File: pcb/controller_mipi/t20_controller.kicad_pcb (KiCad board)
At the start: 2 copper layers, 48 parts, among them J1 M55-7002042R, J2 M55-7002042R, J3 1-84952-5, J4 1-84952-5, J5 0473093351, U10 MIC33153YHJ-TR, U13 NCP161BMX330TBG, U2 MIC33153YHJ-TR, U3 MIC5353-2.8YMT, U4 TPS22964CYZPR, U5 MIC5353-2.5YMT, U6 MIC5353-1.8YMT, U7 TPS22964CYZPR, U8 TPS22964CYZPR, U9 TPS22964CYZPR

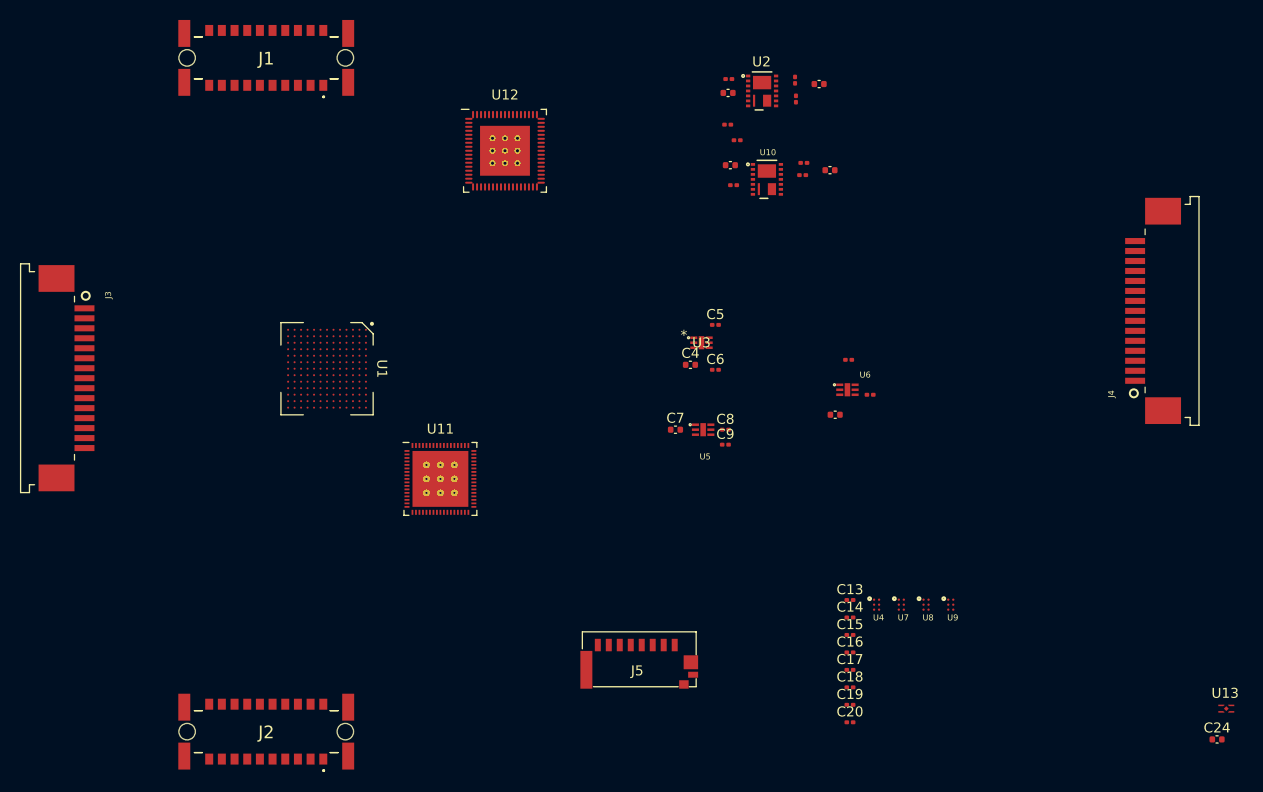
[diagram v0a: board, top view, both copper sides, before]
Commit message: 4 mipi connectors exposed
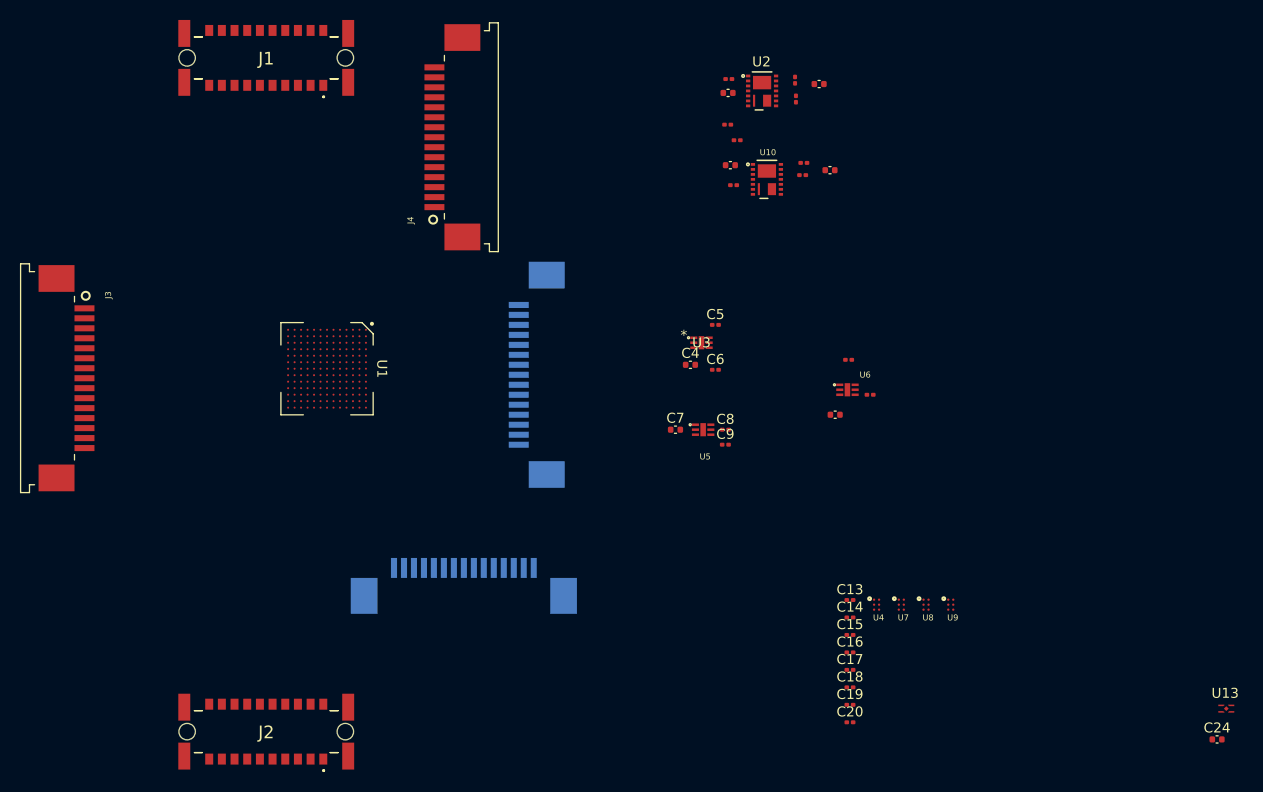
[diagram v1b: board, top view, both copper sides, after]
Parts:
- removed U11: ~, smd:QFN-68_EP_7x7_Pitch0.35mm
- removed U12: ~, smd:QFN-68_EP_8x8_Pitch0.4mm
- added J6: 1-84952-5, smd:TE_1-84952-5, B.Cu at (129.8, 118.3)
- J5: value 0473093351 -> 1-84952-5; footprint smd:0473093351 -> smd:TE_1-84952-5; moved to B.Cu
- moved J4 72.3 mm to (126.8, 75.2)
- moved J5 28.3 mm to (135.3, 99.0), turned to -90 degrees
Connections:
- J3 pad 11: unconnected-(J3-Pad11) -> /MIPI/MIPI0_TXD3_N
- J3 pad 12: unconnected-(J3-Pad12) -> /MIPI/MIPI0_TXD3_P
- J3 pad 13: unconnected-(J3-Pad13) -> GND
- J3 pad 14: unconnected-(J3-Pad14) -> /MIPI/MIPI0_TXD4_N
- J3 pad 15: unconnected-(J3-Pad15) -> /MIPI/MIPI0_TXD4_P
- J4 pad 11: unconnected-(J4-Pad11) -> /MIPI/MIPI0_RXD3_N
- J4 pad 12: unconnected-(J4-Pad12) -> /MIPI/MIPI0_RXD3_P
- J4 pad 13: unconnected-(J4-Pad13) -> GND
- J4 pad 14: unconnected-(J4-Pad14) -> /MIPI/MIPI0_RXD4_N
- J4 pad 15: unconnected-(J4-Pad15) -> /MIPI/MIPI0_RXD4_P
- J5 pad 1: unconnected-(J5-DAT2-Pad1) -> GND
- J5 pad 2: unconnected-(J5-CD/DAT3-Pad2) -> /MIPI/MIPI1_TXD0_N
- J5 pad 3: unconnected-(J5-CMD-Pad3) -> /MIPI/MIPI1_TXD0_P
- J5 pad 4: unconnected-(J5-VDD-Pad4) -> GND
- J5 pad 5: unconnected-(J5-CLK-Pad5) -> /MIPI/MIPI1_TXD1_N
- J5 pad 6: unconnected-(J5-VSS-Pad6) -> /MIPI/MIPI1_TXD1_P
- J5 pad 7: unconnected-(J5-DAT0-Pad7) -> GND
- J5 pad 8: unconnected-(J5-DAT1-Pad8) -> /MIPI/MIPI1_TXD2_N
- U1 pad A10: unconnected-(U1G-MIPI1_TXDP4-PadA10) -> /MIPI/MIPI1_TXD4_P
- U1 pad A11: unconnected-(U1G-MIPI1_RXDN0-PadA11) -> /MIPI/MIPI1_RXD0_N
- U1 pad A12: unconnected-(U1G-MIPI1_RXDN2-PadA12) -> /MIPI/MIPI1_RXD2_N
- U1 pad A4: unconnected-(U1F-MIPI0_TXDP4-PadA4) -> /MIPI/MIPI0_TXD4_P
- U1 pad A7: unconnected-(U1F-MIPI0_RXDN4-PadA7) -> /MIPI/MIPI0_RXD4_N
- U1 pad B10: unconnected-(U1G-MIPI1_TXDN4-PadB10) -> /MIPI/MIPI1_TXD4_N
- U1 pad B11: unconnected-(U1G-MIPI1_RXDP0-PadB11) -> /MIPI/MIPI1_RXD0_P
- U1 pad B12: unconnected-(U1G-MIPI1_RXDP2-PadB12) -> /MIPI/MIPI1_RXD2_P
- U1 pad B13: unconnected-(U1G-MIPI1_RXDN4-PadB13) -> /MIPI/MIPI1_RXD4_N
- U1 pad B4: unconnected-(U1F-MIPI0_TXDN4-PadB4) -> /MIPI/MIPI0_TXD4_N
- U1 pad B7: unconnected-(U1F-MIPI0_RXDP4-PadB7) -> /MIPI/MIPI0_RXD4_P
- U1 pad C10: unconnected-(U1G-MIPI1_RXDP1-PadC10) -> /MIPI/MIPI1_RXD1_P
- U1 pad C12: unconnected-(U1G-MIPI1_RXDP3-PadC12) -> /MIPI/MIPI1_RXD3_P
- U1 pad C13: unconnected-(U1G-MIPI1_RXDP4-PadC13) -> /MIPI/MIPI1_RXD4_P
- U1 pad C5: unconnected-(U1F-MIPI0_TXDP3-PadC5) -> /MIPI/MIPI0_TXD3_P
- U1 pad C7: unconnected-(U1F-MIPI0_RXDP3-PadC7) -> /MIPI/MIPI0_RXD3_P
- U1 pad C9: unconnected-(U1G-MIPI1_TXDP3-PadC9) -> /MIPI/MIPI1_TXD3_P
- U1 pad D1: /FPGA_USB3/HRACT -> /MIC_ARRAY/HRACT
- U1 pad D10: unconnected-(U1G-MIPI1_RXDN1-PadD10) -> /MIPI/MIPI1_RXD1_N
- U1 pad D12: unconnected-(U1G-MIPI1_RXDN3-PadD12) -> /MIPI/MIPI1_RXD3_N
- U1 pad D2: /FPGA_USB3/HRCLK -> /MIC_ARRAY/HRCLK
- U1 pad D5: unconnected-(U1F-MIPI0_TXDN3-PadD5) -> /MIPI/MIPI0_TXD3_N
- U1 pad D7: unconnected-(U1F-MIPI0_RXDN3-PadD7) -> /MIPI/MIPI0_RXD3_N
- U1 pad D9: unconnected-(U1G-MIPI1_TXDN3-PadD9) -> /MIPI/MIPI1_TXD3_N
- U1 pad E1: /FPGA_USB3/HTREQ -> /MIC_ARRAY/HTREQ
- U1 pad F1: /FPGA_USB3/HTCLK -> /MIC_ARRAY/HTCLK
- U1 pad F2: /FPGA_USB3/HTVLD -> /MIC_ARRAY/HTVLD
- U1 pad G2: /FPGA_USB3/HTACK -> /MIC_ARRAY/HTACK
- U1 pad G3: /FPGA_USB3/HRVLD -> /MIC_ARRAY/HRVLD
- U1 pad H3: /FPGA_USB3/HTRDY -> /MIC_ARRAY/HTRDY

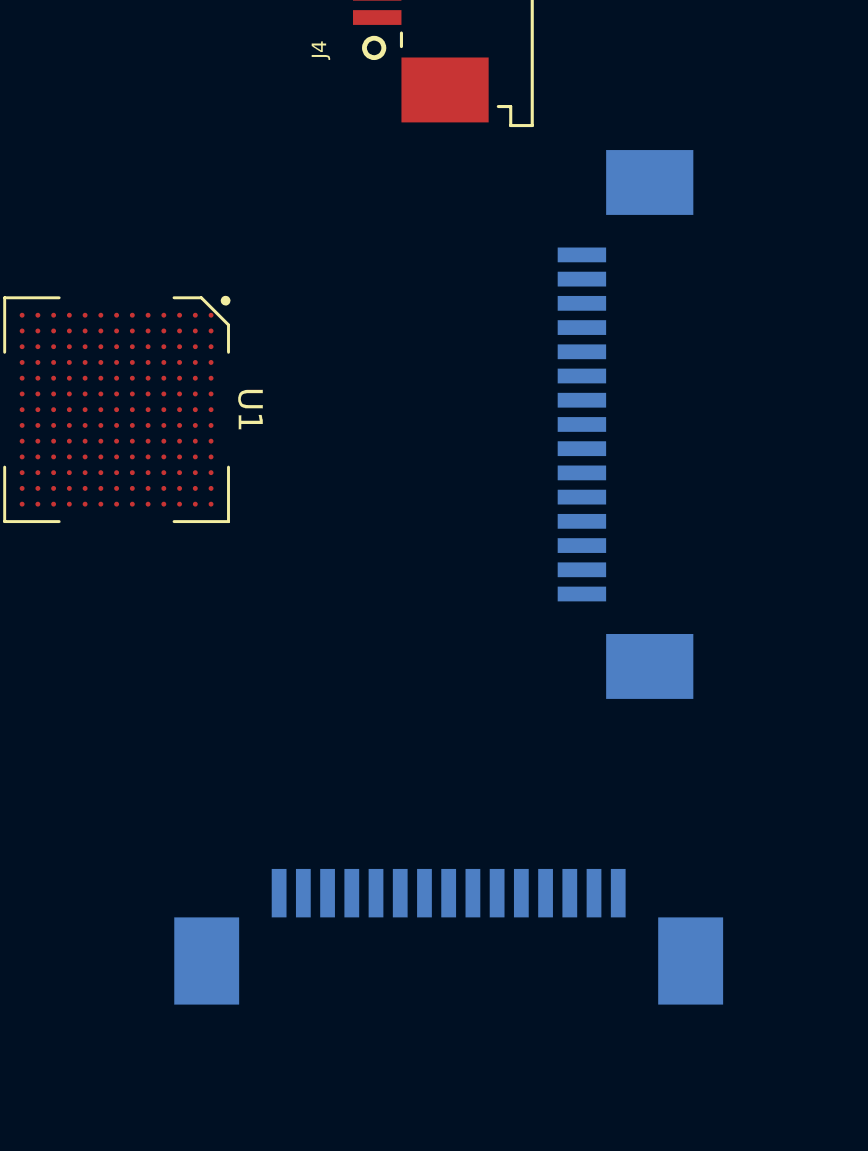
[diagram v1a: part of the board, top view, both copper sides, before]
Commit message: 4 mipi connectors exposed
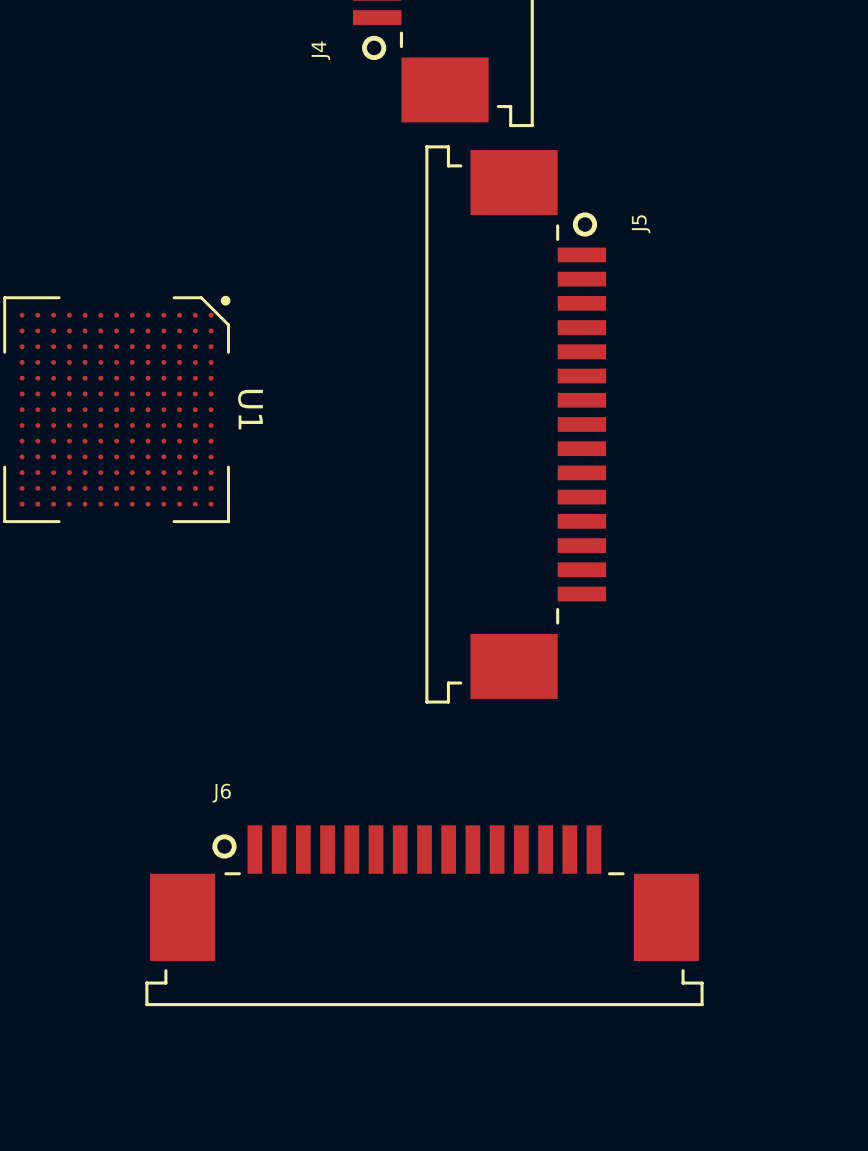
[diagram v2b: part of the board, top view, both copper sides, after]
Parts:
- J5, J6: moved to F.Cu
- moved J6 2.06 mm to (128.8, 116.5), turned to 0 degrees
